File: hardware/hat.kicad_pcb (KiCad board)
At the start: 4 copper layers, 65 x 56.6 mm, 144 parts, among them J101 Raspberry_Pi_2_3, J102 Boot, J201 USB Power In, K201 CONN_3, P101 Debug, P201 Black, P301 CON-SENSOR2, P302 CON-SENSOR2, P303 CON-SENSOR2, P304 CON-SENSOR2, P305 CON-SENSOR2, P306 CON-SENSOR2, P307 CON-SENSOR2, P308 CON-SENSOR2, Q101 2N7002P, Q102 2N7002P, Q103 NTR2101P, Q104 NTR2101P, U101 XMC1404, U102 LD1117, U201 MAX17260_LS, U202 BQ2407X, U203 AOZ1212, U204 MIC2253, U205 AP7333-33SAG-7, U301 74AHC244, U302 74AHC244, U303 74AHC244, U304 74AHC244, X101 32.768kHz

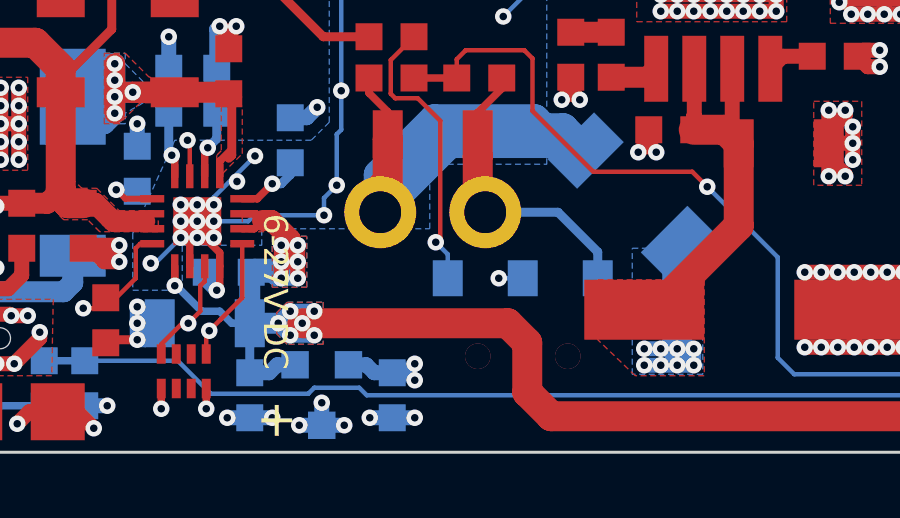
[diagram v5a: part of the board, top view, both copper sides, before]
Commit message: update slide switch footprint
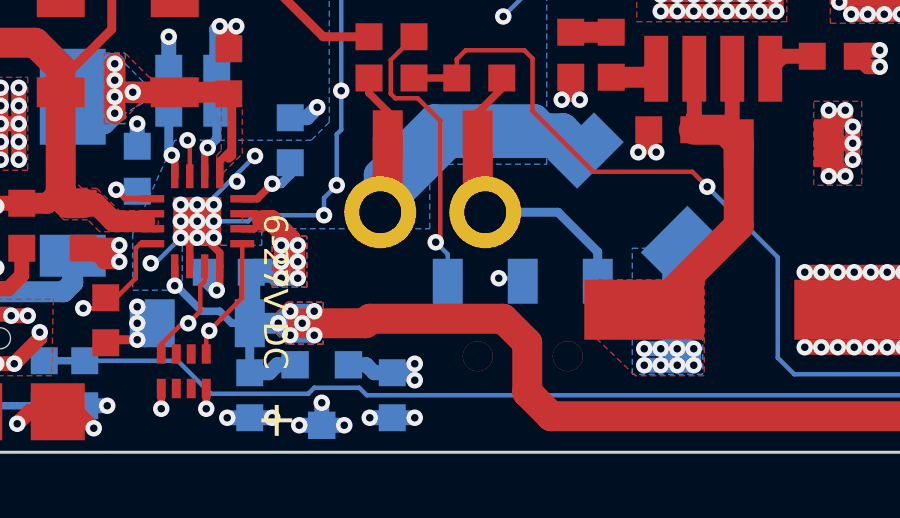
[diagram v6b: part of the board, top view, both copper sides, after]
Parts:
- S201: footprint SW-SLIDE-SMD -> kicad-libraries:SW-SLIDE-SMD
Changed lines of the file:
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@@
     (thickness 1.6)
     (drawings 50)
-    (tracks 3262)
+    (tracks 3264)
     (zones 0)
     (modules 144)
@@
   (layers
     (0 F.Cu signal)
-    (1 GND signal)
+    (1 GND signal hide)
     (2 VCC signal hide)
     (31 B.Cu signal)
@@
   )
   (setup
-    (last_trace_width 0.15)
+    (last_trace_width 1)
     (user_trace_width 0.15)
     (user_trace_width 0.2)
@@
     (aux_axis_origin 166.2 25.4)
     (grid_origin 166.2 25.4)
-    (visible_elements FFFDDF7F)
+    (visible_elements FFFD5F7F)
     (pcbplotparams
       (layerselection 0x010fc_ffffffff)
@@
     (add_net USB-IN-VOLTAGE)
   )
+  (module kicad-libraries:SW-SLIDE-SMD (layer B.Cu)
+    (at 196.2 78.8)
+    (fp_text reference S201 (at 0 -0.5) (layer B.SilkS)
+      (effects (font (size 0.3 0.3) (thickness 0.075)) (justify mirror))
+    )
+    (fp_text value SWITCH_SPDT (at 0 0.5) (layer B.Fab)
+      (effects (font (size 0.3 0.3) (thickness 0.075)) (justify mirror))
+    )
+    (fp_line (start 0.8 1.5) (end 0.8 3) (layer B.Fab) (width 0.1))
+    (fp_line (start 0.8 3) (end -0.8 3) (layer B.Fab) (width 0.1))
+    (fp_line (start -0.8 3) (end -0.8 1.5) (layer B.Fab) (width 0.1))
+    (fp_line (start -2.1 -1.5) (end -2.1 -2.8) (layer B.Fab) (width 0.1))
+    (fp_line (start -2.1 -2.8) (end -2.9 -2.8) (layer B.Fab) (width 0.1))
+    (fp_line (start -2.9 -2.8) (end -2.9 -1.5) (layer B.Fab) (width 0.1))
+    (fp_line (start 0.4 -1.5) (end 0.4 -2.8) (layer B.Fab) (width 0.1))
+    (fp_line (start 0.4 -2.8) (end -0.4 -2.8) (layer B.Fab) (width 0.1))
+    (fp_line (start -0.4 -2.8) (end -0.4 -1.5) (layer B.Fab) (width 0.1))
+    (fp_line (start 2.9 -1.5) (end 2.9 -2.8) (layer B.Fab) (width 0.1))
+    (fp_line (start 2.9 -2.8) (end 2.1 -2.8) (layer B.Fab) (width 0.1))
+    (fp_line (start 2.1 -2.8) (end 2.1 -1.5) (layer B.Fab) (width 0.1))
+    (fp_line (start -3.6 1.5) (end 3.6 1.5) (layer B.Fab) (width 0.1))
+    (fp_line (start 3.6 1.5) (end 3.6 -1.5) (layer B.Fab) (width 0.1))
+    (fp_line (start 3.6 -1.5) (end -3.6 -1.5) (layer B.Fab) (width 0.1))
+    (fp_line (start -3.6 -1.5) (end -3.6 1.5) (layer B.Fab) (width 0.1))
+    (pad 1 smd rect (at -2.5 -2.5) (size 1 1.5) (layers B.Cu B.Paste B.Mask)
+      (net 144 "Net-(R219-Pad1)"))
+    (pad 2 smd rect (at 0 -2.5) (size 1 1.5) (layers B.Cu B.Paste B.Mask)
+      (net 145 SYSOFF))
+    (pad 3 smd rect (at 2.5 -2.5) (size 1 1.5) (layers B.Cu B.Paste B.Mask)
+      (net 2 GND))
+    (pad "" thru_hole circle (at -1.5 0) (size 1 1) (drill 1) (layers *.Cu))
+    (pad "" thru_hole circle (at 1.5 0) (size 1 1) (drill 1) (layers *.Cu))
+  )
   (module kicad-libraries:QFN16-0.5 (layer F.Cu)
     (at 185.35 74.3 270)
@@
     )
   )
-  (module SW-SLIDE-SMD (layer B.Cu)
-    (at 196.2 78.8)
-    (fp_text reference S201 (at 0 -0.5) (layer B.SilkS)
-      (effects (font (size 0.3 0.3) (thickness 0.075)) (justify mirror))
-    )
-    (fp_text value SWITCH_SPDT (at 0 0.5) (layer B.Fab)
-      (effects (font (size 0.3 0.3) (thickness 0.075)) (justify mirror))
-    )
-    (fp_line (start -3.6 -1.5) (end -3.6 1.5) (layer B.Fab) (width 0.1))
-    (fp_line (start 3.6 -1.5) (end -3.6 -1.5) (layer B.Fab) (width 0.1))
-    (fp_line (start 3.6 1.5) (end 3.6 -1.5) (layer B.Fab) (width 0.1))
-    (fp_line (start -3.6 1.5) (end 3.6 1.5) (layer B.Fab) (width 0.1))
-    (fp_line (start 2.1 -2.8) (end 2.1 -1.5) (layer B.Fab) (width 0.1))
-    (fp_line (start 2.9 -2.8) (end 2.1 -2.8) (layer B.Fab) (width 0.1))
-    (fp_line (start 2.9 -1.5) (end 2.9 -2.8) (layer B.Fab) (width 0.1))
-    (fp_line (start -0.4 -2.8) (end -0.4 -1.5) (layer B.Fab) (width 0.1))
-    (fp_line (start 0.4 -2.8) (end -0.4 -2.8) (layer B.Fab) (width 0.1))
-    (fp_line (start 0.4 -1.5) (end 0.4 -2.8) (layer B.Fab) (width 0.1))
-    (fp_line (start -2.9 -2.8) (end -2.9 -1.5) (layer B.Fab) (width 0.1))
-    (fp_line (start -2.1 -2.8) (end -2.9 -2.8) (layer B.Fab) (width 0.1))
-    (fp_line (start -2.1 -1.5) (end -2.1 -2.8) (layer B.Fab) (width 0.1))
-    (fp_line (start -0.8 3) (end -0.8 1.5) (layer B.Fab) (width 0.1))
-    (fp_line (start 0.8 3) (end -0.8 3) (layer B.Fab) (width 0.1))
-    (fp_line (start 0.8 1.5) (end 0.8 3) (layer B.Fab) (width 0.1))
-    (pad "" thru_hole circle (at 1.5 0) (size 0.85 0.85) (drill 0.85) (layers *.Cu))
-    (pad "" thru_hole circle (at -1.5 0) (size 0.85 0.85) (drill 0.85) (layers *.Cu))
-    (pad 3 smd rect (at 2.5 -2.6) (size 1 1.2) (layers B.Cu B.Paste B.Mask)
-      (net 2 GND))
-    (pad 2 smd rect (at 0 -2.6) (size 1 1.2) (layers B.Cu B.Paste B.Mask)
-      (net 145 SYSOFF))
-    (pad 1 smd rect (at -2.5 -2.6) (size 1 1.2) (layers B.Cu B.Paste B.Mask)
-      (net 144 "Net-(R219-Pad1)"))
-  )
   (module kicad-libraries:AB26TRQ (layer F.Cu)
     (at 227.4 41.55)
@@
   (segment (start 219.7 74.5) (end 216.45 74.5) (width 1) (layer F.Cu) (net 125))
   (segment (start 216.59886 78.25) (end 216.59886 74.64886) (width 1) (layer F.Cu) (net 125))
-  (segment (start 215.2 80.8) (end 216.59886 79.40114) (width 1) (layer F.Cu) (net 125))
-  (segment (start 216.59886 79.40114) (end 216.59886 78.25) (width 1) (layer F.Cu) (net 125))
+  (segment (start 196.35 78.35) (end 196.35 80) (width 1) (layer F.Cu) (net 125))
+  (segment (start 196.35 80) (end 197.15 80.8) (width 1) (layer F.Cu) (net 125))
+  (segment (start 197.15 80.8) (end 215.2 80.8) (width 1) (layer F.Cu) (net 125))
   (segment (start 216.59886 74.64886) (end 216.45 74.5) (width 1) (layer F.Cu) (net 125))
+  (segment (start 216.59886 79.40114) (end 216.59886 78.25) (width 1) (layer F.Cu) (net 125))
+  (segment (start 215.2 80.8) (end 216.59886 79.40114) (width 1) (layer F.Cu) (net 125))
   (via (at 188.85 77.7) (size 0.55) (drill 0.25) (layers F.Cu B.Cu) (net 125))
   (segment (start 188.05 77.7) (end 188.85 77.7) (width 0.5) (layer B.Cu) (net 125))
@@
   (segment (start 184.6007 76.4493) (end 184.6 76.45) (width 0.25) (layer F.Cu) (net 125))
   (via (at 184.6 76.45) (size 0.55) (drill 0.25) (layers F.Cu B.Cu) (net 125))
-  (segment (start 188.85 77.7) (end 195.7 77.7) (width 1) (layer F.Cu) (net 125))
-  (segment (start 197.15 80.8) (end 215.2 80.8) (width 1) (layer F.Cu) (net 125))
-  (segment (start 196.35 80) (end 197.15 80.8) (width 1) (layer F.Cu) (net 125))
-  (segment (start 196.35 78.35) (end 196.35 80) (width 1) (layer F.Cu) (net 125))
-  (segment (start 195.7 77.7) (end 196.35 78.35) (width 1) (layer F.Cu) (net 125))
+  (segment (start 188.85 77.7) (end 190.95 77.7) (width 1) (layer F.Cu) (net 125))
+  (segment (start 195.55 77.55) (end 196.35 78.35) (width 1) (layer F.Cu) (net 125))
+  (segment (start 191.1 77.55) (end 195.55 77.55) (width 1) (layer F.Cu) (net 125))
+  (segment (start 190.95 77.7) (end 191.1 77.55) (width 1) (layer F.Cu) (net 125))
   (segment (start 183.2 70) (end 181.95036 70) (width 0.7) (layer B.Cu) (net 126))
   (segment (start 183.20114 70.00114) (end 183.2 70) (width 0.7) (layer F.Cu) (net 126))

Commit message: specify crystal capacitors 10pF
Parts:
- C105, C106: value TBD -> 10pF
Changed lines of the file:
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@@
   )
   (setup
-    (last_trace_width 1)
+    (last_trace_width 0.15)
     (user_trace_width 0.15)
     (user_trace_width 0.2)
@@
     (aux_axis_origin 166.2 25.4)
     (grid_origin 166.2 25.4)
-    (visible_elements FFFD5F7F)
+    (visible_elements FFFFDF7F)
     (pcbplotparams
       (layerselection 0x010fc_ffffffff)
@@
       (effects (font (size 0.2 0.2) (thickness 0.05)))
     )
-    (fp_text value TBD (at 0.05 -0.375 270) (layer F.Fab)
+    (fp_text value 10pF (at 0.05 -0.375 270) (layer F.Fab)
       (effects (font (size 0.2 0.2) (thickness 0.05)))
     )
@@
       (effects (font (size 0.2 0.2) (thickness 0.05)))
     )
-    (fp_text value TBD (at 0.05 -0.375 270) (layer F.Fab)
-      (effects (font (size 0.2 0.2) (thickness 0.05)))
-    )
+    (fp_text value 10pF (at 0.05 -0.375 270) (layer F.Fab)
+      (effects (font (size 0.2 0.2) (thickness 0.05)))
+    )

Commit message: add bug hint
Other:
- board text added: "RASP-EN/B-EN -> P2.8/P2.9"
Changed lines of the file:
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@@
   (general
     (thickness 1.6)
-    (drawings 50)
+    (drawings 51)
     (tracks 3264)
     (zones 0)
@@
     )
   )
+  (gr_text "RASP-EN/B-EN -> P2.8/P2.9" (at 196.6 93.3) (layer Dwgs.User)
+    (effects (font (size 2.032 1.524) (thickness 0.3048)))
+  )
   (gr_text "Add Switch Text" (at 194.4 84.65) (layer Dwgs.User)
